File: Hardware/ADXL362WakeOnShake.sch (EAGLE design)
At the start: 23 parts, among them J1 PROG_HDR, U1 ADXL362, U3 ADP160-3.3

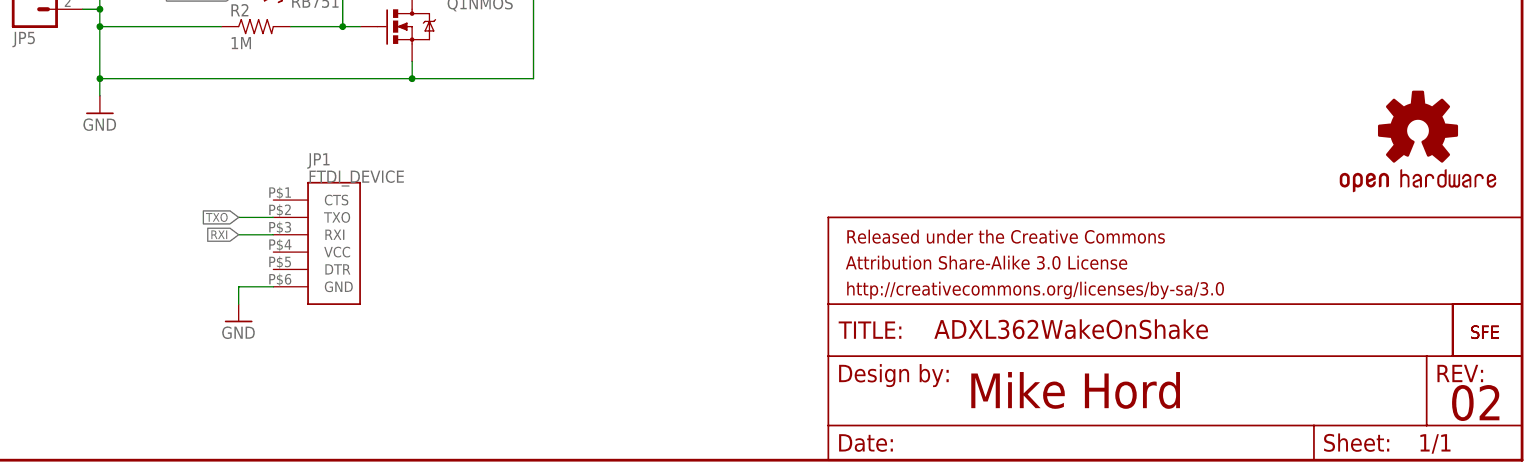
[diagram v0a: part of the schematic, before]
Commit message: Updating hardware files to v10: - FTDI header silk changed to accurately reflect pin names - moved some traces to avoid silk/via collision - added 10k resistor pull-up on RX line - FTDI header was slightly off grid - added silk on ATTiny package.
Changes to Firmware are purely machine changes to project files.
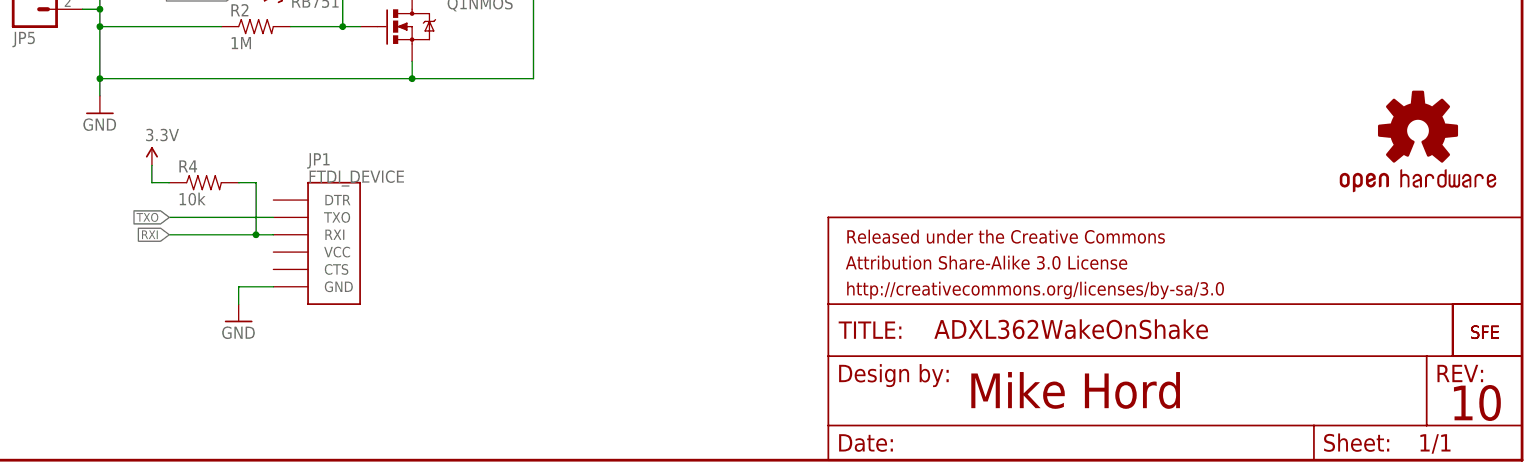
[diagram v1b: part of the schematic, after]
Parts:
- added R4: 10k, SparkFun-Passives:RESISTOR0402-RES
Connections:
- net 3.3V: now also R4.1
- net RXI: now also R4.2
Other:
- note added: "10"
- note removed: "02"
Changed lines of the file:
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@@
 <part name="JP6" library="SparkFun-Aesthetics" deviceset="LOGO-SFE" device="NEW"/>
 <part name="JP7" library="SparkFun-Connectors" deviceset="M05" device="PTH"/>
+<part name="R4" library="SparkFun-Passives" deviceset="RESISTOR" device="0402-RES" value="10k">
+<attribute name="PROD_ID" value="RES-00824"/>
+</part>
+<part name="P+7" library="SparkFun-Aesthetics" deviceset="3.3V" device=""/>
 </parts>
 <sheets>
@@
 <plain>
 <text x="167.64" y="7.62" size="5.08" layer="94">Mike Hord</text>
-<text x="238.252" y="5.842" size="5.08" layer="94">02</text>
+<text x="238.252" y="5.842" size="5.08" layer="94">10</text>
 </plain>
 <instances>
@@
 <instance part="JP6" gate="G$1" x="241.3" y="17.78"/>
 <instance part="JP7" gate="G$1" x="154.94" y="139.7" rot="R180"/>
+<instance part="R4" gate="G$1" x="55.88" y="40.64">
+<attribute name="PROD_ID" x="55.88" y="40.64" size="1.778" layer="96" display="off"/>
+</instance>
+<instance part="P+7" gate="G$1" x="48.26" y="43.18"/>
 </instances>
 <busses>
@@
 <pinref part="R3" gate="G$1" pin="1"/>
 </segment>
+<segment>
+<pinref part="P+7" gate="G$1" pin="3.3V"/>
+<wire x1="48.26" y1="43.18" x2="48.26" y2="40.64" width="0.1524" layer="91"/>
+<pinref part="R4" gate="G$1" pin="1"/>
+<wire x1="48.26" y1="40.64" x2="50.8" y2="40.64" width="0.1524" layer="91"/>
+</segment>
 </net>
 <net name="SCK" class="0">
@@
 <segment>
 <pinref part="JP1" gate="G$1" pin="RXI"/>
-<wire x1="66.04" y1="33.02" x2="60.96" y2="33.02" width="0.1524" layer="91"/>
-<label x="60.96" y="33.02" size="1.27" layer="95" rot="R180" xref="yes"/>
+<wire x1="66.04" y1="33.02" x2="63.5" y2="33.02" width="0.1524" layer="91"/>
+<label x="50.8" y="33.02" size="1.27" layer="95" rot="R180" xref="yes"/>
+<pinref part="R4" gate="G$1" pin="2"/>
+<wire x1="63.5" y1="33.02" x2="50.8" y2="33.02" width="0.1524" layer="91"/>
+<wire x1="60.96" y1="40.64" x2="63.5" y2="40.64" width="0.1524" layer="91"/>
+<wire x1="63.5" y1="40.64" x2="63.5" y2="33.02" width="0.1524" layer="91"/>
+<junction x="63.5" y="33.02"/>
 </segment>
 </net>
@@
 <segment>
 <pinref part="JP1" gate="G$1" pin="TXO"/>
-<wire x1="66.04" y1="35.56" x2="60.96" y2="35.56" width="0.1524" layer="91"/>
-<label x="60.96" y="35.56" size="1.27" layer="95" rot="R180" xref="yes"/>
-</segment>
-</net>
+<wire x1="66.04" y1="35.56" x2="50.8" y2="35.56" width="0.1524" layer="91"/>
+<label x="50.8" y="35.56" size="1.27" layer="95" rot="R180" xref="yes"/>
+</segment>
+</net>
